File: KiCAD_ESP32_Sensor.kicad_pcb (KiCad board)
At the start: 2 copper layers, 32.7 x 40 mm, 29 parts, among them J1 USB_C_Receptacle_USB2.0_16P, J2 VL53L0X_Module, Q1 MMBT3904, Q2 MMBT3904, U1 CH340C, U2 AMS1117-3.3, U3 ESP32-WROOM-32E

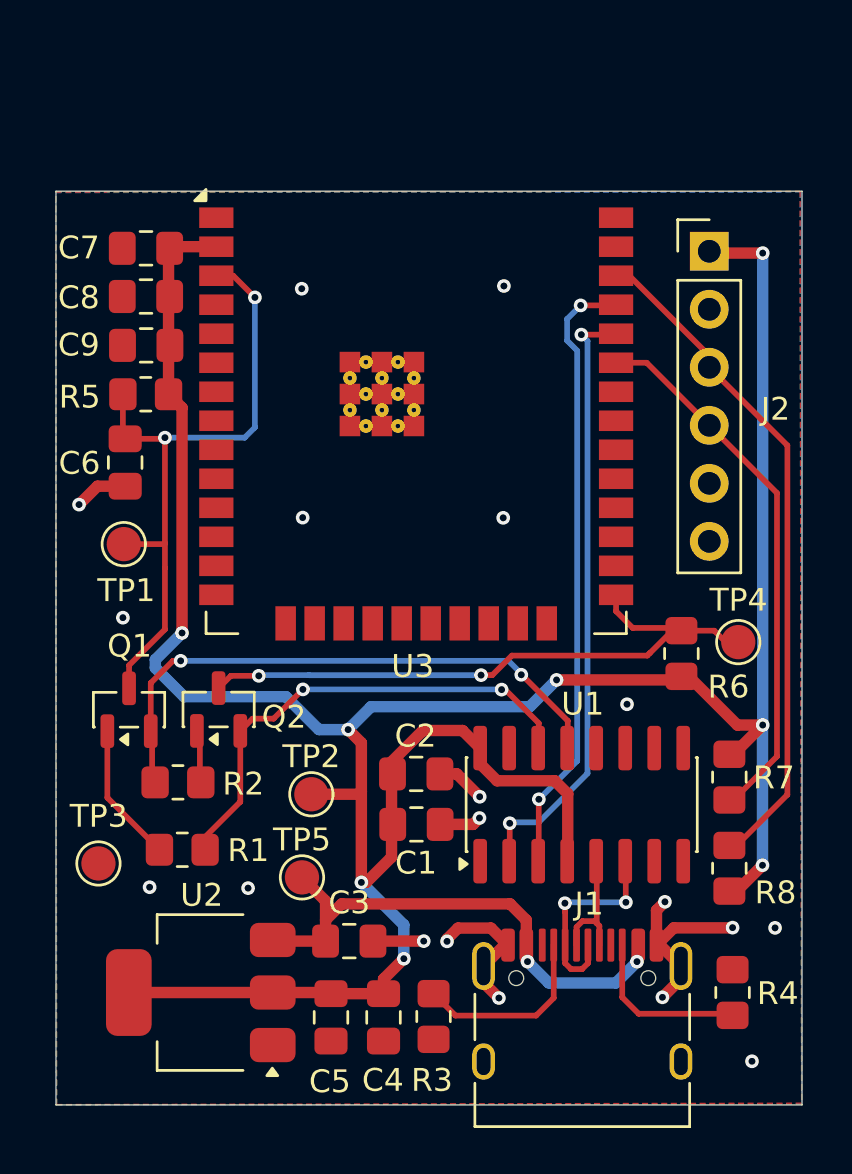
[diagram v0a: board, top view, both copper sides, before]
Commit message: Finalized: components & pcb purchased
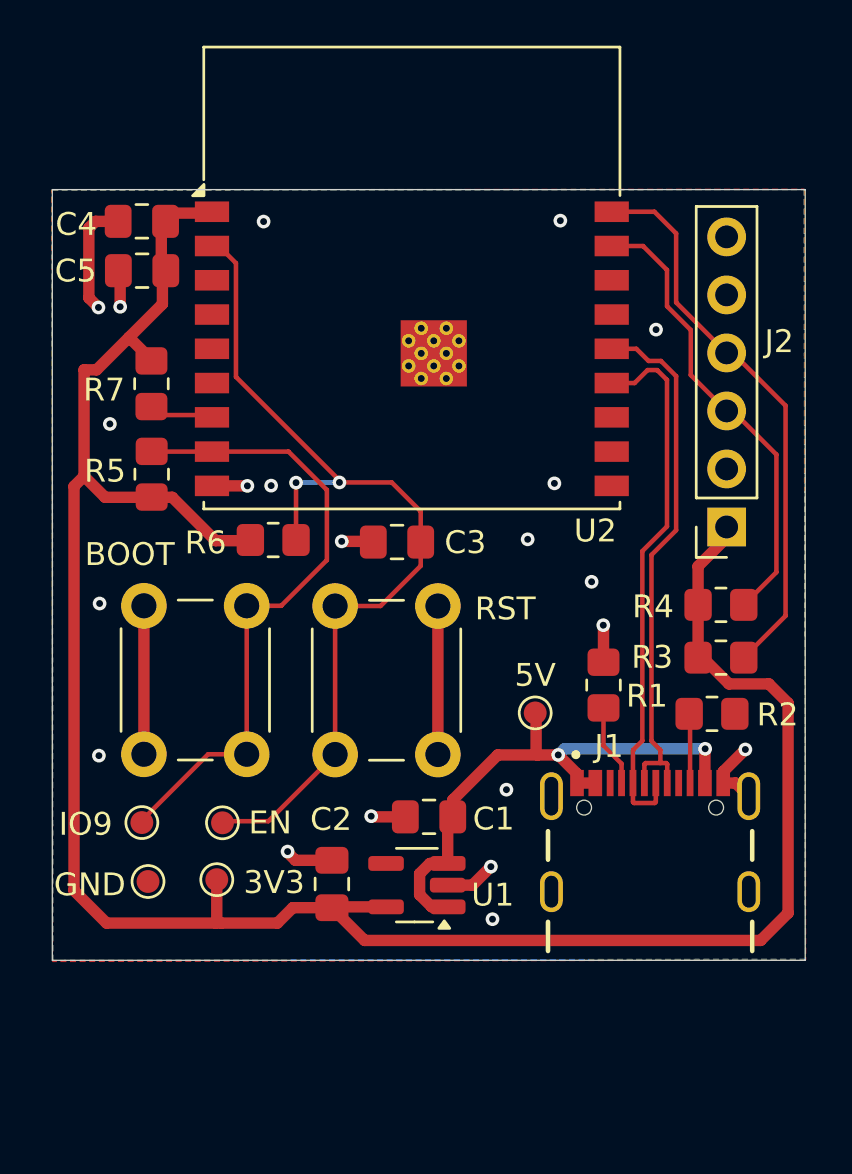
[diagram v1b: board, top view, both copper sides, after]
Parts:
- removed C6, C8: 1u, Capacitor_SMD:C_0805_2012Metric_Pad1.18x1.45mm_HandSolder
- removed C7: 0.1u, Capacitor_SMD:C_0805_2012Metric_Pad1.18x1.45mm_HandSolder
- removed C9: 10u, Capacitor_SMD:C_0805_2012Metric_Pad1.18x1.45mm_HandSolder
- removed Q1, Q2: MMBT3904, Package_TO_SOT_SMD:SOT-23
- removed R8: 4.7k, Resistor_SMD:R_0805_2012Metric_Pad1.20x1.40mm_HandSolder
- removed TP1, TP2, TP3, TP4, TP5: TestPoint, TestPoint:TestPoint_Pad_D1.5mm
- removed U3: ESP32-WROOM-32E, RF_Module:ESP32-WROOM-32E
- added 3V3: 3.3V, TestPoint:TestPoint_Pad_D1.0mm, F.Cu at (59.0, 80.3)
- added 5V: 5V, TestPoint:TestPoint_Pad_D1.0mm, F.Cu at (72.9, 73.0)
- added BOOT: SW_Push, Button_Switch_THT:SW_PUSH_6mm_H5mm, F.Cu at (60.3, 68.3)
- added EN: EN, TestPoint:TestPoint_Pad_D1.0mm, F.Cu at (59.2, 77.8)
- added GND: GND, TestPoint:TestPoint_Pad_D1.0mm, F.Cu at (56.0, 80.4)
- added IO9: IO0, TestPoint:TestPoint_Pad_D1.0mm, F.Cu at (55.7, 77.8)
- added RST: SW_Push, Button_Switch_THT:SW_PUSH_6mm_H5mm, F.Cu at (64.2, 74.9)
- C1, C3: value 10u -> 1u
- C2: value 0.1u -> 1u
- C4: value 10u -> 0.1u
- C5: value 0.1u -> 10u
- J1: footprint Connector_USB:USB_C_Receptacle_HRO_TYPE-C-31-M-12 -> USBC:GCT_USB4105-GF-A
- J2: footprint Connector_PinHeader_2.54mm:PinHeader_1x06_P2.54mm_Vertical -> Connector_PinSocket_2.54mm:PinSocket_1x06_P2.54mm_Vertical
- R1, R2: value 10k -> 5.1k
- R3, R4: value 5.1k -> 4.7k
- R7: value 4.7k -> 10k
- U1: value CH340C -> AP2112K-3.3; footprint Package_SO:SOIC-16_3.9x9.9mm_P1.27mm -> Package_TO_SOT_SMD:SOT-23-5_HandSoldering
- U2: value AMS1117-3.3 -> ESP32-C3-WROOM-02; footprint Package_TO_SOT_SMD:SOT-223-3_TabPin2 -> RF_Module:ESP32-C3-WROOM-02
- moved C4 36.4 mm to (55.7, 51.5), turned to 180 degrees
- moved C5 33.7 mm to (55.7, 53.7), turned to 180 degrees
- moved R7 30.6 mm to (56.1, 58.6), turned to -90 degrees
- moved U2 29.7 mm to (67.5, 57.1), turned to 0 degrees
- moved R2 23.6 mm to (80.7, 73.1)
- moved R3 20.1 mm to (81.1, 70.6), turned to 180 degrees
- moved R1 19.8 mm to (75.9, 71.8), turned to -90 degrees
- moved R6 18.5 mm to (61.5, 65.5), turned to 0 degrees
- moved C3 17.6 mm to (66.9, 65.6)
- moved R4 17.0 mm to (81.1, 68.3), turned to 180 degrees
- moved J2 12.1 mm to (81.3, 64.9), turned to 180 degrees
- moved U1 8.03 mm to (67.8, 80.6), turned to 180 degrees
- moved J1 7.04 mm to (78.0, 80.9)
- moved C2 6.07 mm to (64.0, 80.5), turned to 90 degrees
- moved R5 3.51 mm to (56.1, 62.6), turned to 90 degrees
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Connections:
- C1 pad 1: +3.3V -> +5V
- C2 pad 1: GND -> +3.3V
- C2 pad 2: +3.3V -> GND
- C3 pad 1: +5V -> GND
- C3 pad 2: GND -> EN
- J1 pad A6: USB_D_PLUS -> D+
- J1 pad A7: USB_D_MINUS -> D-
- J1 pad B6: USB_D_PLUS -> D+
- J1 pad B7: USB_D_MINUS -> D-
- R1 pad 1: Net-(Q1-B) -> GND
- R1 pad 2: RTS -> Net-(J1-CC1)
- R2 pad 1: Net-(Q2-B) -> GND
- R2 pad 2: DTR -> Net-(J1-CC2)
- R3 pad 1: GND -> SDA
- R3 pad 2: Net-(J1-CC1) -> +3.3V
- R4 pad 1: GND -> SCL
- R4 pad 2: Net-(J1-CC2) -> +3.3V
- R5 pad 2: EN -> IO9
- R6 pad 2: IO0 -> EN
- R7 pad 1: SDA -> +3.3V
- R7 pad 2: +3.3V -> Net-(U2-IO8)
- U1 pad 1: GND -> +5V
- U1 pad 2: TXD -> GND
- U1 pad 3: RXD -> +5V
- U1 pad 4: +3.3V -> unconnected-(U1-NC-Pad4)
- U1 pad 5: USB_D_PLUS -> +3.3V
- U2 pad 1: GND -> +3.3V
- U2 pad 2: +3.3V -> EN
- U2 pad 3: +5V -> unconnected-(U2-IO4-Pad3)
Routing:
- net IO9: track 0.00 -> 28.5 mm
- net IO0: track 27.5 -> 0.00 mm, vias 2 -> 0
- net RXD: track 26.3 -> 0.00 mm, vias 2 -> 0
- net TXD: track 26.1 -> 0.00 mm, vias 2 -> 0
- net +3.3V: track 126.8 -> 102.2 mm, vias 8 -> 0
- net DTR: track 24.7 -> 0.00 mm, vias 2 -> 0
- net D-: track 0.00 -> 23.8 mm
- net D+: track 0.00 -> 23.6 mm
- net RTS: track 20.8 -> 0.00 mm, vias 2 -> 0
- net EN: track 29.0 -> 40.7 mm
- net GND: track 22.5 -> 33.3 mm, vias 19 -> 21
- net USB_D_MINUS: track 9.78 -> 0.00 mm, vias 2 -> 0
- net SCL: track 28.3 -> 19.8 mm
- net USB_D_PLUS: track 6.33 -> 0.00 mm
- net Net-(Q1-B): track 6.06 -> 0.00 mm
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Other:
- board size 32.7 x 40 mm -> 33 x 33.7 mm
